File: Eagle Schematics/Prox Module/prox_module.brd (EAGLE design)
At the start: 64.4 x 80 mm, 45 parts, among them IC1 74LS14N, IC2 74LS14N, Q1 16MHZ

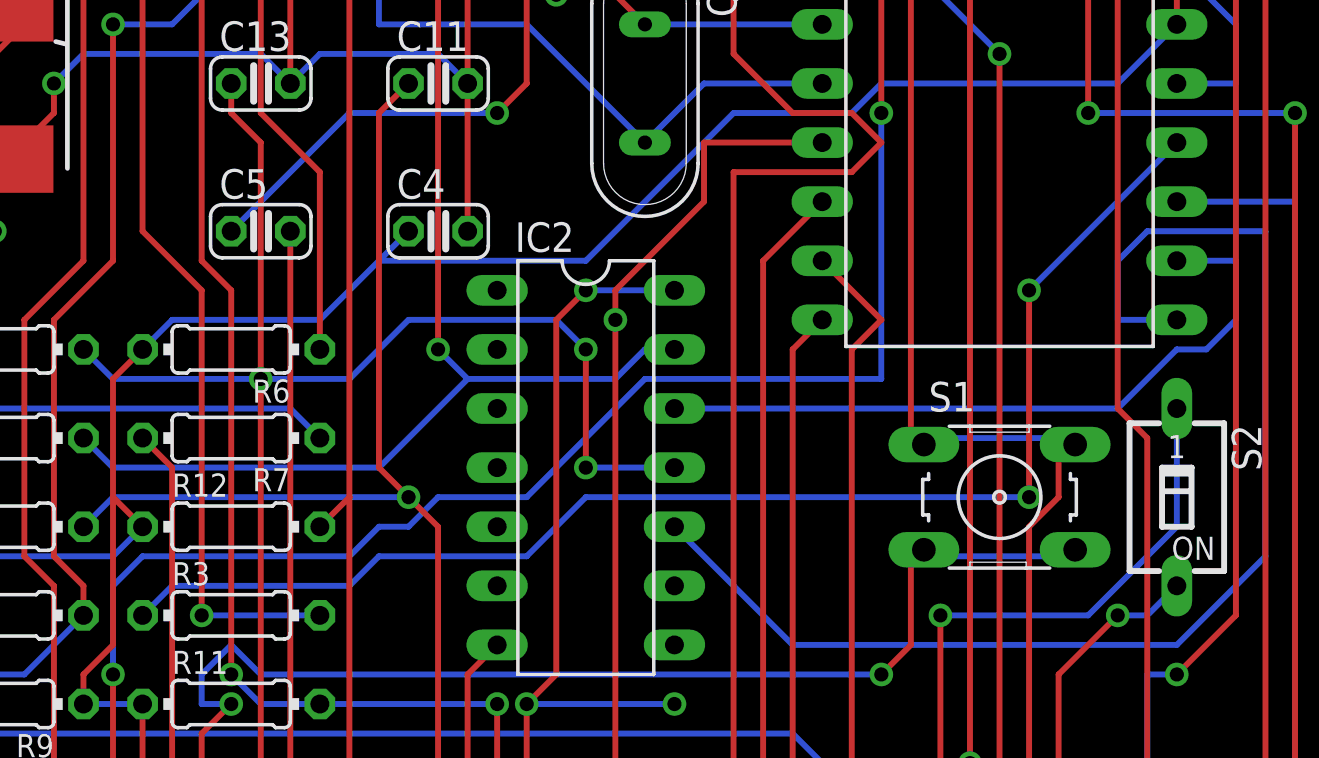
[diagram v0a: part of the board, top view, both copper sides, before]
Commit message: Fixed issue with level converter
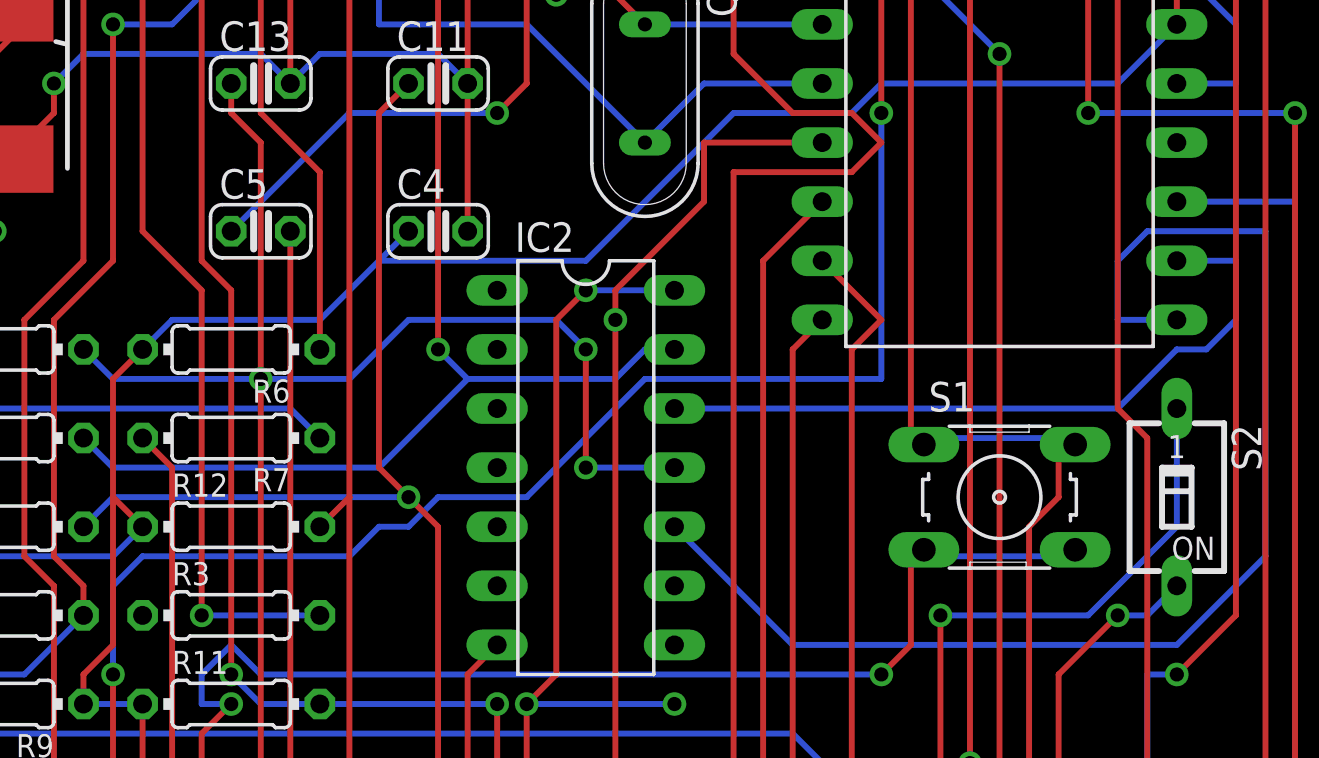
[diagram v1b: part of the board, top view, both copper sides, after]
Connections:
- removed net I2C-EN-1: AT328.18, R3.1
- net 3V: now also R3.1
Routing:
- net I2C-EN-1: track 58.1 -> 0.00 mm, vias 2 -> 0
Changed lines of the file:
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@@
 <wire x1="13.97" y1="21.59" x2="13.97" y2="38.1" width="0.254" layer="1"/>
 <wire x1="12.7" y1="20.32" x2="13.97" y2="21.59" width="0.254" layer="1"/>
+<contactref element="R3" pad="1"/>
+<wire x1="13.97" y1="38.1" x2="12.7" y2="31.75" width="0" layer="19" extent="1-1"/>
 </signal>
 <signal name="SCL">
@@
 <via x="15.24" y="31.75" extent="1-16" drill="0.6096"/>
 </signal>
-<signal name="I2C-EN-1">
-<contactref element="R3" pad="1"/>
-<contactref element="AT328" pad="18"/>
-<via x="50.8" y="36.83" extent="1-16" drill="0.6096"/>
-<wire x1="31.75" y1="36.83" x2="50.8" y2="36.83" width="0.254" layer="16"/>
-<wire x1="29.21" y1="34.29" x2="31.75" y2="36.83" width="0.254" layer="16"/>
-<wire x1="22.86" y1="34.29" x2="29.21" y2="34.29" width="0.254" layer="16"/>
-<wire x1="21.59" y1="33.02" x2="22.86" y2="34.29" width="0.254" layer="16"/>
-<wire x1="13.97" y1="33.02" x2="21.59" y2="33.02" width="0.254" layer="16"/>
-<wire x1="12.7" y1="31.75" x2="13.97" y2="33.02" width="0.254" layer="16"/>
-<wire x1="50.8" y1="45.72" x2="57.15" y2="52.07" width="0.254" layer="16"/>
-<wire x1="50.8" y1="36.83" x2="50.8" y2="45.72" width="0.254" layer="1"/>
-<via x="50.8" y="45.72" extent="1-16" drill="0.6096"/>
-</signal>
 <signal name="SDA-5V">
